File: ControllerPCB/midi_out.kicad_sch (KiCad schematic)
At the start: 4 parts, among them J14 MIDI Out Conn, U3 74LVC1G17

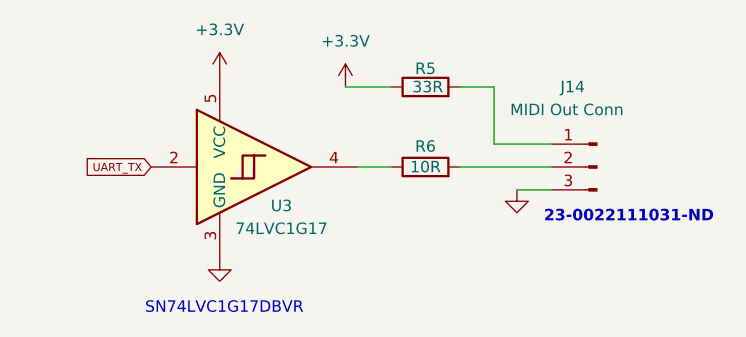
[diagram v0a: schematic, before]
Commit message: Added VCAP 1/2 capacitors. These assist the internal voltage regulator. We don't have an option to turn the regulator off so it is always on.
Swapped the crystal oscillator out for a different one.

Tweaked the VREF+ scheme a bit - changed the 100nF decoupling cap to 10nF to comply with the datasheet when VREF+ is connected to VDDA
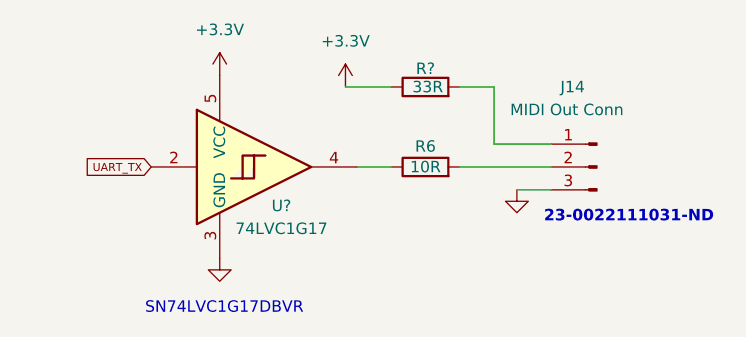
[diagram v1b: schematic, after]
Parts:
- renumbered R5 to R?, U3 to U?
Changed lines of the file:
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@@
 		(dnp no)
 		(fields_autoplaced yes)
-		(property "Reference" "#PWR033"
+		(property "Reference" "#PWR?"
 			(at 113.03 68.58 0)
 			(effects
@@
 		(pin "1"
 		)
+		(instances
+			(project "ControllerPCB"
+				(path "/b6b9154e-ee88-44ea-8b68-6c4328b55066/3d1f8010-af48-4a48-807c-a6cd14f7ebca"
+					(reference "#PWR?")
+					(unit 1)
+				)
+			)
+		)
 	)
 	(symbol
@@
 		(on_board yes)
 		(dnp no)
-		(property "Reference" "R5"
+		(property "Reference" "R?"
 			(at 102.87 48.768 90)
 			(effects
@@
 		)
 		(pin "2"
+		)
+		(instances
+			(project "ControllerPCB"
+				(path "/b6b9154e-ee88-44ea-8b68-6c4328b55066/3d1f8010-af48-4a48-807c-a6cd14f7ebca"
+					(reference "R?")
+					(unit 1)
+				)
+			)
 		)
 	)
@@
 		(on_board yes)
 		(dnp no)
-		(property "Reference" "U3"
+		(property "Reference" "U?"
 			(at 86.868 64.008 0)
 			(effects
@@
 		(pin "4"
 		)
-	)
+		(instances
+			(project "ControllerPCB"
+				(path "/b6b9154e-ee88-44ea-8b68-6c4328b55066/3d1f8010-af48-4a48-807c-a6cd14f7ebca"
+					(reference "U?")
+					(unit 1)
+				)
+			)
+		)
+	)

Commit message: Organized the schematic a bit
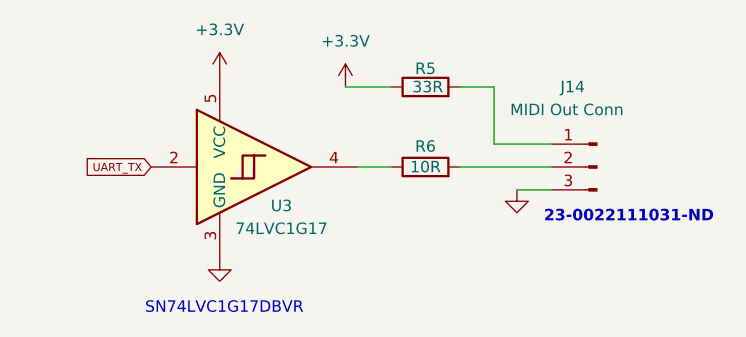
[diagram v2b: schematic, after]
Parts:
- gave numbers to parts that had none: 2
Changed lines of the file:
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@@
 		(dnp no)
 		(fields_autoplaced yes)
-		(property "Reference" "#PWR?"
+		(property "Reference" "#PWR0101"
 			(at 113.03 68.58 0)
 			(effects
@@
 			(project "ControllerPCB"
 				(path "/b6b9154e-ee88-44ea-8b68-6c4328b55066/3d1f8010-af48-4a48-807c-a6cd14f7ebca"
-					(reference "#PWR?")
+					(reference "#PWR0101")
 					(unit 1)
 				)
@@
 		(on_board yes)
 		(dnp no)
-		(property "Reference" "R?"
+		(property "Reference" "R5"
 			(at 102.87 48.768 90)
 			(effects
@@
 			(project "ControllerPCB"
 				(path "/b6b9154e-ee88-44ea-8b68-6c4328b55066/3d1f8010-af48-4a48-807c-a6cd14f7ebca"
-					(reference "R?")
+					(reference "R5")
 					(unit 1)
 				)
@@
 		(on_board yes)
 		(dnp no)
-		(property "Reference" "U?"
+		(property "Reference" "U3"
 			(at 86.868 64.008 0)
 			(effects
@@
 			(project "ControllerPCB"
 				(path "/b6b9154e-ee88-44ea-8b68-6c4328b55066/3d1f8010-af48-4a48-807c-a6cd14f7ebca"
-					(reference "U?")
-					(unit 1)
-				)
+					(reference "U3")
+					(unit 1)
+				)

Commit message: Began the PCB. Placed the decoupling caps, usb micro b conn and others. Adding footprints for components as well.
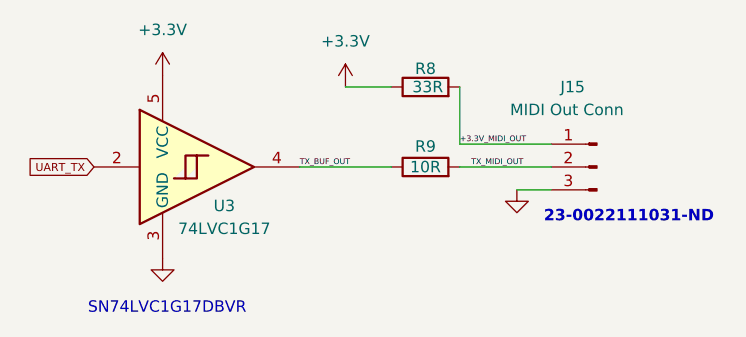
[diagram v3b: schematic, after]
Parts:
- J15: renamed from J14; footprint (none) -> 22292031:CONN_AE-6410-03A_MOL
- R8: renamed from R5; footprint (none) -> Resistor_SMD:R_0402_1005Metric
- R9: renamed from R6; footprint (none) -> Resistor_SMD:R_0402_1005Metric
- U3: footprint (none) -> SN74LVC1G17DBVR:SOT95P280X145-5N
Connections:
- net +3.3V_MIDI_OUT: now reaches J15.1 (Pin_1), R8.2
- net TX_BUF_OUT: now reaches R9.1, U3.4
- net TX_MIDI_OUT: now reaches J15.2 (Pin_2), R9.2
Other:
- moved on the sheet: U3

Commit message: Added separate sheet for IO. Added TVS diodes for every external input to the controller except for the ADC and MIDI control inputs. Still need to add decoupling caps for the 9V humbucker source. Parts were chosen with JLPCB library stock in mind. Replaced the 8MHz crystal with a 16MHz crystal.
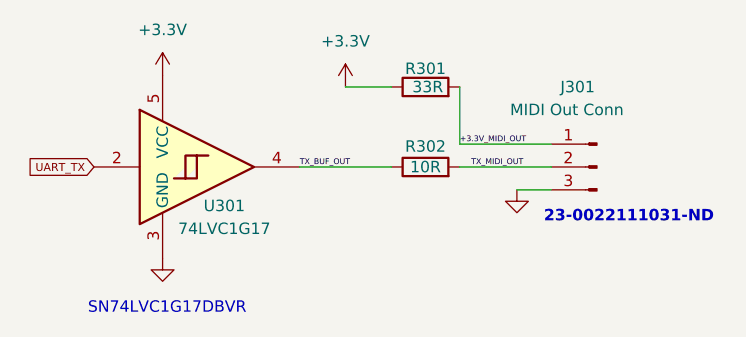
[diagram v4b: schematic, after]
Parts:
- renumbered J15 to J301, R8 to R301, R9 to R302, U3 to U301
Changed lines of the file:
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@@
 		(dnp no)
 		(fields_autoplaced yes)
-		(property "Reference" "#PWR038"
+		(property "Reference" "#PWR0302"
 			(at 73.66 76.2 0)
 			(effects
@@
 			(project "ControllerPCB"
 				(path "/b6b9154e-ee88-44ea-8b68-6c4328b55066/3d1f8010-af48-4a48-807c-a6cd14f7ebca"
-					(reference "#PWR038")
+					(reference "#PWR0302")
 					(unit 1)
 				)
@@
 		(dnp no)
 		(fields_autoplaced yes)
-		(property "Reference" "#PWR040"
+		(property "Reference" "#PWR0304"
 			(at 113.03 68.58 0)
 			(effects
@@
 			(project "ControllerPCB"
 				(path "/b6b9154e-ee88-44ea-8b68-6c4328b55066/3d1f8010-af48-4a48-807c-a6cd14f7ebca"
-					(reference "#PWR040")
+					(reference "#PWR0304")
 					(unit 1)
 				)
@@
 		(on_board yes)
 		(dnp no)
-		(property "Reference" "R8"
+		(property "Reference" "R301"
 			(at 102.87 48.768 90)
 			(effects
@@
 			(project "ControllerPCB"
 				(path "/b6b9154e-ee88-44ea-8b68-6c4328b55066/3d1f8010-af48-4a48-807c-a6cd14f7ebca"
-					(reference "R8")
+					(reference "R301")
 					(unit 1)
 				)
@@
 		(on_board yes)
 		(dnp no)
-		(property "Reference" "#PWR039"
+		(property "Reference" "#PWR0303"
 			(at 93.98 54.61 0)
 			(effects
@@
 			(project "ControllerPCB"
 				(path "/b6b9154e-ee88-44ea-8b68-6c4328b55066/3d1f8010-af48-4a48-807c-a6cd14f7ebca"
-					(reference "#PWR039")
+					(reference "#PWR0303")
 					(unit 1)
 				)
@@
 		(on_board yes)
 		(dnp no)
-		(property "Reference" "#PWR037"
+		(property "Reference" "#PWR0301"
 			(at 73.66 53.34 0)
 			(effects
@@
 			(project "ControllerPCB"
 				(path "/b6b9154e-ee88-44ea-8b68-6c4328b55066/3d1f8010-af48-4a48-807c-a6cd14f7ebca"
-					(reference "#PWR037")
+					(reference "#PWR0301")
 					(unit 1)
 				)
@@
 		(on_board yes)
 		(dnp no)
-		(property "Reference" "R9"
+		(property "Reference" "R302"
 			(at 102.87 57.404 90)
 			(effects
@@
 			(project "ControllerPCB"
 				(path "/b6b9154e-ee88-44ea-8b68-6c4328b55066/3d1f8010-af48-4a48-807c-a6cd14f7ebca"
-					(reference "R9")
+					(reference "R302")
 					(unit 1)
 				)
@@
 		(on_board yes)
 		(dnp no)
-		(property "Reference" "J15"
+		(property "Reference" "J301"
 			(at 117.856 50.8 0)
 			(effects
@@
 			(project "ControllerPCB"
 				(path "/b6b9154e-ee88-44ea-8b68-6c4328b55066/3d1f8010-af48-4a48-807c-a6cd14f7ebca"
-					(reference "J15")
+					(reference "J301")
 					(unit 1)
 				)
@@
 		(on_board yes)
 		(dnp no)
-		(property "Reference" "U3"
+		(property "Reference" "U301"
 			(at 80.518 64.008 0)
 			(effects
@@
 			(project "ControllerPCB"
 				(path "/b6b9154e-ee88-44ea-8b68-6c4328b55066/3d1f8010-af48-4a48-807c-a6cd14f7ebca"
-					(reference "U3")
-					(unit 1)
-				)
+					(reference "U301")
+					(unit 1)
+				)

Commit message: rev 0.3
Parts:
- J301: footprint 22292031:CONN_AE-6410-03A_MOL -> 0_Footprint_lib:CONN_AE-6410-03A_MOL
- U301: footprint SN74LVC1G17DBVR:SOT95P280X145-5N -> 0_Footprint_lib:SOT95P280X145-5N
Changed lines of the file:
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@@
 		(effects
 			(font
-				(size 0.635 0.635)
+				(size 0.889 0.889)
 			)
 			(justify left bottom)
@@
 		(effects
 			(font
-				(size 0.635 0.635)
+				(size 1.143 1.143)
 			)
 			(justify left bottom)
@@
 		(effects
 			(font
-				(size 0.635 0.635)
+				(size 0.889 0.889)
 			)
 			(justify left bottom)
@@
 			)
 		)
-		(property "Footprint" "22292031:CONN_AE-6410-03A_MOL"
+		(property "Footprint" "0_Footprint_lib:CONN_AE-6410-03A_MOL"
 			(at 121.92 59.69 0)
 			(effects
@@
 			)
 		)
-		(property "Footprint" "SN74LVC1G17DBVR:SOT95P280X145-5N"
+		(property "Footprint" "0_Footprint_lib:SOT95P280X145-5N"
 			(at 76.2 59.69 0)
 			(effects

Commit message: rev 1.04
- gerbers/BOM/CPL files are all generated.
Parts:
- J301: now not fitted; now left out of the parts list
- R301: JLCPCB Part # (none) -> C25105
- R302: JLCPCB Part # (none) -> C25077
- U301: JLCPCB Part # (none) -> C7836
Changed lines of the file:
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@@
+			)
+		)
+		(property "JLCPCB Part #" "C25105"
+			(at 102.87 50.8 0)
+			(effects
+				(font
+					(size 1.27 1.27)
+				)
+				(hide yes)
 			)
 		)
@@
 			)
 		)
+		(property "JLCPCB Part #" "C25077"
+			(at 102.87 59.69 0)
+			(effects
+				(font
+					(size 1.27 1.27)
+				)
+				(hide yes)
+			)
+		)
 		(pin "1"
 		)
@@
 		(unit 1)
 		(exclude_from_sim no)
-		(in_bom yes)
-		(on_board yes)
-		(dnp no)
+		(in_bom no)
+		(on_board yes)
+		(dnp yes)
 		(property "Reference" "J301"
 			(at 117.856 50.8 0)
@@
 		)
 		(property "Description" "Generic connector, single row, 01x03, script generated"
+			(at 121.92 59.69 0)
+			(effects
+				(font
+					(size 1.27 1.27)
+				)
+				(hide yes)
+			)
+		)
+		(property "JLCPCB Part #" ""
 			(at 121.92 59.69 0)
 			(effects
@@
 			(at 78.74 59.69 0)
 			(effects
+				(font
+					(size 1.27 1.27)
+				)
+				(hide yes)
+			)
+		)
+		(property "JLCPCB Part #" "C7836"
+			(at 78.74 59.69 0)
+			(effects
